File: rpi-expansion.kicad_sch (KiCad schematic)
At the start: 3 parts, among them J7 PinSocket_2x20_P2.54mm_Drill1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, J8 JST_SH_1x4_SM04B-SRSS-TB-LF-SN, J9 JST_SH_1x4_SM04B-SRSS-TB-LF-SN

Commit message: [#94684] Revise component placement
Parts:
- removed J7: PinSocket_2x20_P2.54mm_Drill1.02mm, antmicro-footprints:PinSocket_2x20_P2.54mm_Drill1.02mm, symbol antmicroGenericPinSockets:PinSocket_2x20_P2.54mm_Drill1.02mm
- added J7: PinHeader_2x20_P2.54mm_Drill1.1mm, antmicro-footprints:PinHeader_2x20_P2.54mm_Drill1.1mm, symbol antmicroGenericPinHeaders:PinHeader_2x20_P2.54mm_Drill1.1mm
- added R4, R5, R6, R7: R_0R_0402, antmicro-footprints:R_0402_1005Metric, symbol antmicroResistors0402:R_0R_0402
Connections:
- net I2C_QWIIC.SCL: now reaches J9.1
- net I2C_QWIIC.SCL: now also J8.1
- net I2C_QWIIC.SDA: now reaches J9.2
- net I2C_QWIIC.SDA: now also J8.2
- net QWIIC_VCC2: now reaches J9.3
- net QWIIC_VCC2: now also R6.1, R7.1
- net GND: now reaches J9.4
- net GND: now also J8.4, J8.MP, J9.MP, J7.14, J7.20, J7.25, J7.30, J7.34, J7.39, J7.6, J7.9
- net QWIIC_VCC1: now reaches J8.3
- net QWIIC_VCC1: now also R4.1, R5.1
- new net +3V3: J7.1, R5.2, R7.2
- new net +5V: J7.2, J7.4, R4.2, R6.2
- new net GPIO4: J7.7
- new net I2C_RPI.SCL: J7.5
- new net I2C_RPI.SDA: J7.3
- new net SPI_RPI.CS0: J7.24
- new net SPI_RPI.CS1: J7.26
- new net SPI_RPI.MISO: J7.21
- new net SPI_RPI.MOSI: J7.19
- new net SPI_RPI.SCK: J7.23
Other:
- moved on the sheet: J8, J9

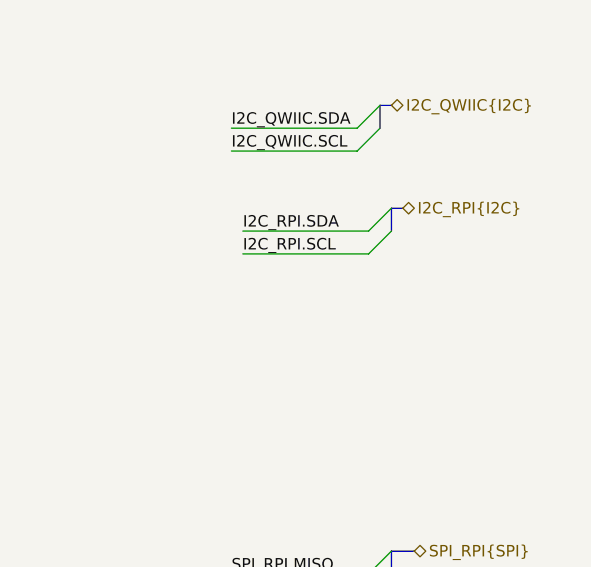
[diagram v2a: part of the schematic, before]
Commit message: [#94727] Add RMII, IOs, JTAG, UART, QSPI connection to MCU
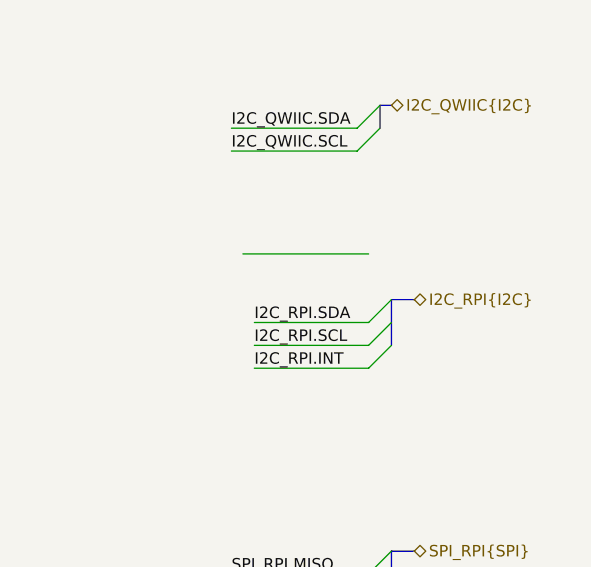
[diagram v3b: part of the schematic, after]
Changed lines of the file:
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@@
 	)
 	(bus_entry
-		(at 308.61 80.01)
+		(at 308.61 92.71)
 		(size -2.54 2.54)
 		(stroke
@@
 	)
 	(bus_entry
+		(at 308.61 95.25)
+		(size -2.54 2.54)
+		(stroke
+			(width 0)
+			(type default)
+		)
+	)
+	(bus_entry
 		(at 308.61 120.65)
 		(size -2.54 2.54)
@@
 	)
 	(bus_entry
-		(at 308.61 125.73)
+		(at 308.61 90.17)
 		(size -2.54 2.54)
 		(stroke
@@
 	)
 	(bus_entry
-		(at 308.61 123.19)
+		(at 308.61 125.73)
 		(size -2.54 2.54)
 		(stroke
@@
 	)
 	(bus_entry
-		(at 308.61 82.55)
+		(at 308.61 123.19)
 		(size -2.54 2.54)
 		(stroke
@@
 		)
 	)
+	(wire
+		(pts
+			(xy 306.07 92.71) (xy 293.37 92.71)
+		)
+		(stroke
+			(width 0)
+			(type default)
+		)
+	)
 	(bus
 		(pts
@@
 	(wire
 		(pts
+			(xy 306.07 95.25) (xy 293.37 95.25)
+		)
+		(stroke
+			(width 0)
+			(type default)
+		)
+	)
+	(wire
+		(pts
 			(xy 262.89 36.83) (xy 259.08 36.83)
 		)
@@
 		)
 	)
-	(bus
-		(pts
-			(xy 309.88 80.01) (xy 308.61 80.01)
-		)
-		(stroke
-			(width 0)
-			(type default)
-		)
-	)
 	(wire
 		(pts
@@
 	(wire
 		(pts
-			(xy 271.78 36.83) (xy 283.21 36.83)
+			(xy 306.07 97.79) (xy 293.37 97.79)
 		)
 		(stroke
@@
 	(wire
 		(pts
-			(xy 292.1 82.55) (xy 306.07 82.55)
+			(xy 271.78 36.83) (xy 283.21 36.83)
 		)
 		(stroke
@@
 	(bus
 		(pts
-			(xy 308.61 80.01) (xy 308.61 82.55)
+			(xy 307.34 68.58) (xy 307.34 71.12)
 		)
 		(stroke
@@
 		)
 	)
-	(bus
+	(wire
 		(pts
-			(xy 307.34 68.58) (xy 307.34 71.12)
+			(xy 259.08 36.83) (xy 259.08 31.75)
 		)
 		(stroke
@@
 	(wire
 		(pts
-			(xy 259.08 36.83) (xy 259.08 31.75)
+			(xy 123.19 104.14) (xy 134.62 104.14)
 		)
 		(stroke
@@
 		)
 	)
-	(wire
+	(bus
 		(pts
-			(xy 123.19 104.14) (xy 134.62 104.14)
+			(xy 311.15 90.17) (xy 308.61 90.17)
+		)
+		(stroke
+			(width 0)
+			(type default)
+		)
+	)
+	(bus
+		(pts
+			(xy 308.61 90.17) (xy 308.61 92.71)
 		)
 		(stroke
@@
 		)
 	)
+	(bus
+		(pts
+			(xy 308.61 92.71) (xy 308.61 95.25)
+		)
+		(stroke
+			(width 0)
+			(type default)
+		)
+	)
 	(wire
 		(pts
@@
 		)
 	)
-	(label "I2C_RPI.SCL"
-		(at 292.1 85.09 0)
-		(effects
-			(font
-				(size 1.27 1.27)
-			)
-			(justify left bottom)
-		)
-	)
 	(label "SPI_RPI.CS0"
 		(at 290.83 128.27 0)
@@
 		)
 	)
-	(label "I2C_RPI.SDA"
-		(at 292.1 82.55 0)
+	(label "I2C_RPI.INT"
+		(at 293.37 97.79 0)
 		(effects
 			(font
@@
 		)
 	)
+	(label "I2C_RPI.SDA"
+		(at 293.37 92.71 0)
+		(effects
+			(font
+				(size 1.27 1.27)
+			)
+			(justify left bottom)
+		)
+	)
 	(label "SPI_RPI.MISO"
 		(at 118.11 124.46 0)
@@
 		)
 	)
+	(label "I2C_RPI.SCL"
+		(at 293.37 95.25 0)
+		(effects
+			(font
+				(size 1.27 1.27)
+			)
+			(justify left bottom)
+		)
+	)
 	(label "I2C_RPI.SDA"
 		(at 123.19 101.6 0)
@@
 	(hierarchical_label "I2C_RPI{I2C}"
 		(shape bidirectional)
-		(at 309.88 80.01 0)
+		(at 311.15 90.17 0)
 		(effects
 			(font

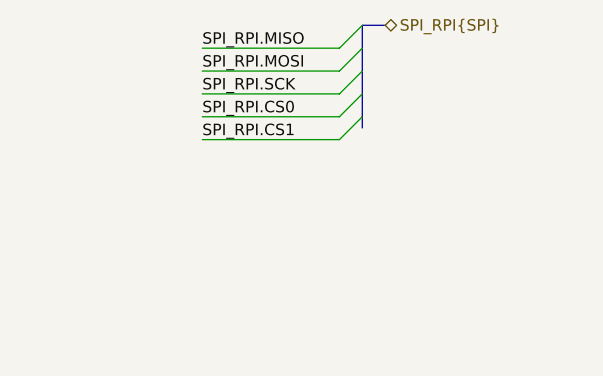
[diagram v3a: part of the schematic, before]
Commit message: [94727] Add remaining I2C buses
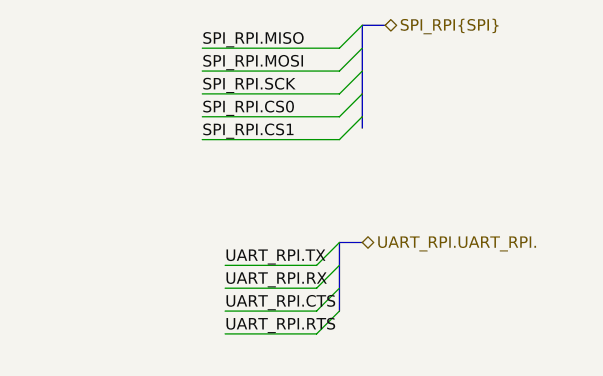
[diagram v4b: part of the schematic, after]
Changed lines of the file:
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@@
 	)
 	(bus_entry
+		(at 306.07 149.86)
+		(size -2.54 2.54)
+		(stroke
+			(width 0)
+			(type default)
+		)
+	)
+	(bus_entry
 		(at 308.61 120.65)
 		(size -2.54 2.54)
@@
 	)
 	(bus_entry
+		(at 306.07 142.24)
+		(size -2.54 2.54)
+		(stroke
+			(width 0)
+			(type default)
+		)
+	)
+	(bus_entry
+		(at 306.07 144.78)
+		(size -2.54 2.54)
+		(stroke
+			(width 0)
+			(type default)
+		)
+	)
+	(bus_entry
 		(at 308.61 123.19)
 		(size -2.54 2.54)
@@
 		)
 	)
+	(bus_entry
+		(at 306.07 147.32)
+		(size -2.54 2.54)
+		(stroke
+			(width 0)
+			(type default)
+		)
+	)
 	(wire
 		(pts
@@
 	(wire
 		(pts
+			(xy 293.37 147.32) (xy 303.53 147.32)
+		)
+		(stroke
+			(width 0)
+			(type default)
+		)
+	)
+	(wire
+		(pts
 			(xy 298.45 36.83) (xy 294.64 36.83)
 		)
@@
 		)
 	)
+	(bus
+		(pts
+			(xy 306.07 147.32) (xy 306.07 149.86)
+		)
+		(stroke
+			(width 0)
+			(type default)
+		)
+	)
 	(wire
 		(pts
@@
 	(wire
 		(pts
+			(xy 293.37 149.86) (xy 303.53 149.86)
+		)
+		(stroke
+			(width 0)
+			(type default)
+		)
+	)
+	(wire
+		(pts
 			(xy 144.78 101.6) (xy 148.59 101.6)
 		)
@@
 	(wire
 		(pts
+			(xy 293.37 144.78) (xy 303.53 144.78)
+		)
+		(stroke
+			(width 0)
+			(type default)
+		)
+	)
+	(wire
+		(pts
 			(xy 290.83 128.27) (xy 306.07 128.27)
 		)
@@
 	(wire
 		(pts
+			(xy 293.37 152.4) (xy 303.53 152.4)
+		)
+		(stroke
+			(width 0)
+			(type default)
+		)
+	)
+	(wire
+		(pts
 			(xy 267.97 39.37) (xy 271.78 39.37)
 		)
@@
 		)
 	)
+	(bus
+		(pts
+			(xy 308.61 142.24) (xy 306.07 142.24)
+		)
+		(stroke
+			(width 0)
+			(type default)
+		)
+	)
 	(wire
 		(pts
@@
 		)
 	)
+	(bus
+		(pts
+			(xy 306.07 142.24) (xy 306.07 144.78)
+		)
+		(stroke
+			(width 0)
+			(type default)
+		)
+	)
 	(wire
 		(pts
@@
 		)
 	)
+	(bus
+		(pts
+			(xy 306.07 144.78) (xy 306.07 147.32)
+		)
+		(stroke
+			(width 0)
+			(type default)
+		)
+	)
 	(image
 		(at 64.77 123.19)
@@
 		)
 	)
+	(label "UART_RPI.RTS"
+		(at 293.37 152.4 0)
+		(effects
+			(font
+				(size 1.27 1.27)
+			)
+			(justify left bottom)
+		)
+	)
 	(label "I2C_RPI.SDA"
 		(at 293.37 92.71 0)
@@
 		)
 	)
+	(label "UART_RPI.RX"
+		(at 293.37 147.32 0)
+		(effects
+			(font
+				(size 1.27 1.27)
+			)
+			(justify left bottom)
+		)
+	)
+	(label "UART_RPI.TX"
+		(at 293.37 144.78 0)
+		(effects
+			(font
+				(size 1.27 1.27)
+			)
+			(justify left bottom)
+		)
+	)
 	(label "SPI_RPI.MISO"
 		(at 118.11 124.46 0)
@@
 		)
 	)
+	(label "UART_RPI.CTS"
+		(at 293.37 149.86 0)
+		(effects
+			(font
+				(size 1.27 1.27)
+			)
+			(justify left bottom)
+		)
+	)
 	(label "I2C_RPI.SDA"
 		(at 123.19 101.6 0)
@@
 		(effects
 			(font
+				(size 1.27 1.27)
+			)
+			(justify left)
+		)
+	)
+	(hierarchical_label "UART_RPI.UART_RPI."
+		(shape bidirectional)
+		(at 308.61 142.24 0)
+		(effects
+			(font

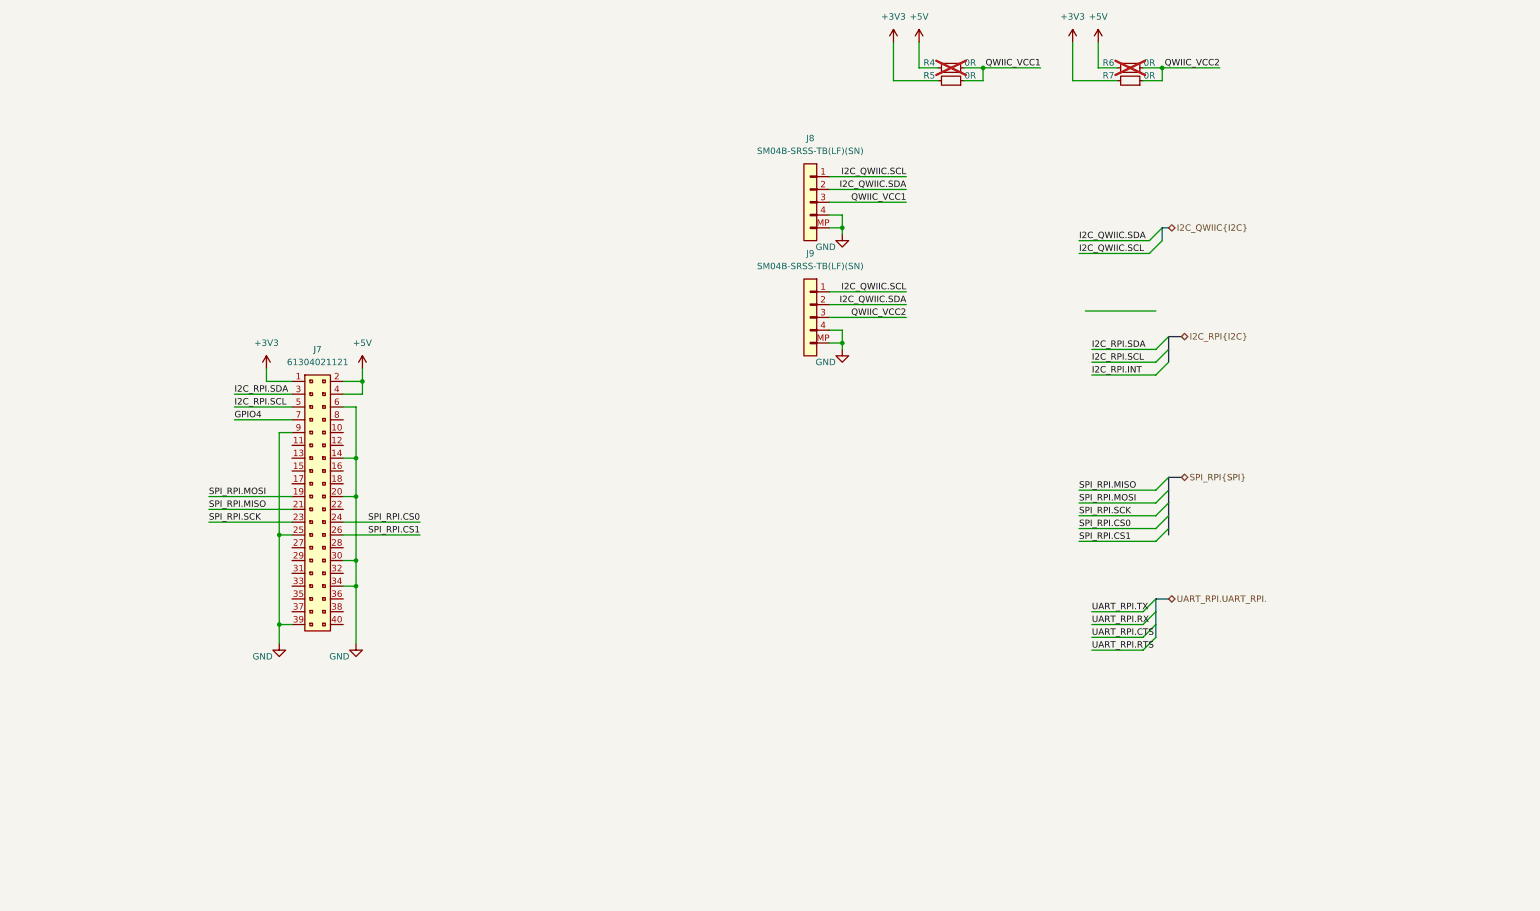
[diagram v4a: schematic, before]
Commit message: [#95036] Reconnect power flags, add GPIOs to RPI connector
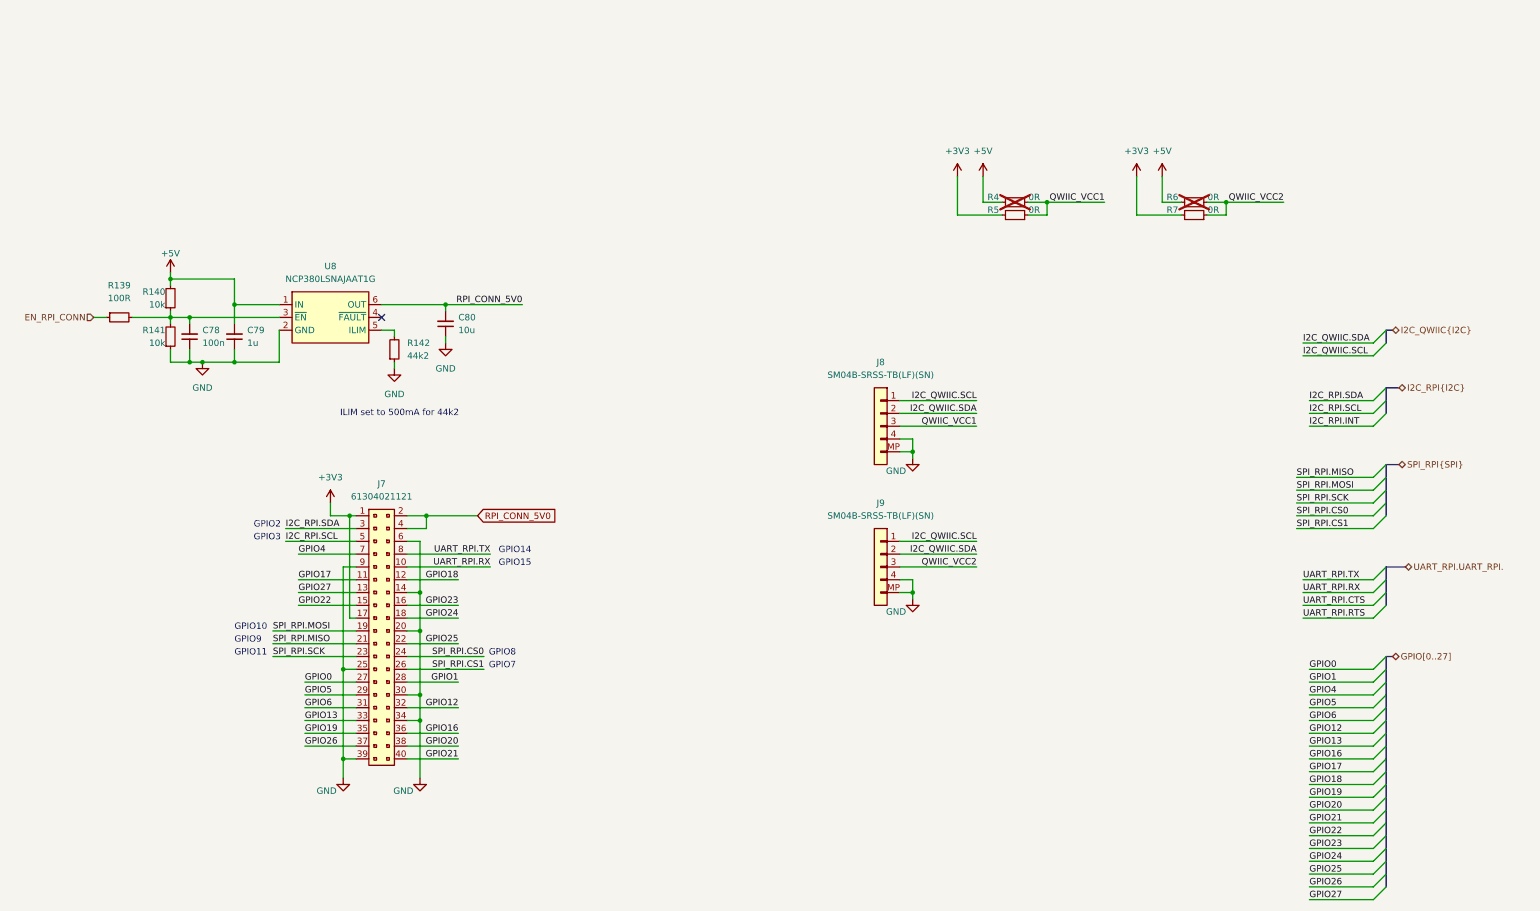
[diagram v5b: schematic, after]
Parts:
- added C78: C_100n_0402, antmicro-footprints:C_0402_1005Metric, symbol antmicroCapacitors0402:C_100n_0402
- added C79: C_1u_0402, antmicro-footprints:C_0402_1005Metric, symbol antmicroCapacitors0402:C_1u_0402
- added C80: C_10u_0402, antmicro-footprints:C_0402_1005Metric, symbol antmicroCapacitors0402:C_10u_0402
- added R139: R_100R_0402, antmicro-footprints:R_0402_1005Metric, symbol antmicroResistors0402:R_100R_0402
- added R140, R141: R_10k_0402, antmicro-footprints:R_0402_1005Metric, symbol antmicroResistors0402:R_10k_0402
- added R142: R_44k2_0402, antmicro-footprints:R_0402_1005Metric, symbol antmicroResistors0402:R_44k2_0402
- added U8: NCP380LSNAJAAT1G, antmicro-footprints:SOT-23-6, symbol antmicroPMICPowerDistributionSwitchesLoadDrivers:NCP380LSNAJAAT1G
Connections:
- net +3V3: now also J7.17
- net +5V: now also C79.2, R140.2, U8.1 (IN); no longer J7.2, J7.4
- net GND: now also C78.1, C79.1, C80.1, R141.1, R142.1, U8.2 (GND)
- net UART_RPI.RX: now also J7.10
- net UART_RPI.TX: now also J7.8
- net GPIO17: now reaches J7.11
- net GPIO18: now reaches J7.12
- net GPIO27: now reaches J7.13
- net GPIO22: now reaches J7.15
- net GPIO23: now reaches J7.16
- net GPIO24: now reaches J7.18
- net GPIO25: now reaches J7.22
- net GPIO0: now reaches J7.27
- net GPIO1: now reaches J7.28
- net GPIO5: now reaches J7.29
- net GPIO6: now reaches J7.31
- net GPIO12: now reaches J7.32
- net GPIO13: now reaches J7.33
- net GPIO19: now reaches J7.35
- net GPIO16: now reaches J7.36
- net GPIO26: now reaches J7.37
- net GPIO20: now reaches J7.38
- net GPIO21: now reaches J7.40
- new net: C78.2, R139.2, R140.1, R141.2, U8.3 (~{EN})
- new net: R142.2, U8.5 (ILIM)
- new net EN_RPI_CONN: R139.1
- new net RPI_CONN_5V0: C80.2, J7.2, J7.4, U8.6 (OUT)
- no-connect marks 0 -> 1
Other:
- note added: "GPIO10"
- note added: "GPIO11"
- note added: "GPIO14"
- note added: "GPIO15"
- note added: "GPIO2"
- note added: "GPIO3"
- note added: "GPIO7"
- note added: "GPIO8"
- note added: "GPIO9"
- note added: "ILIM set to 500mA for 44k2"
- moved on the sheet: J7, J8, J9, R4, R5, R6, R7

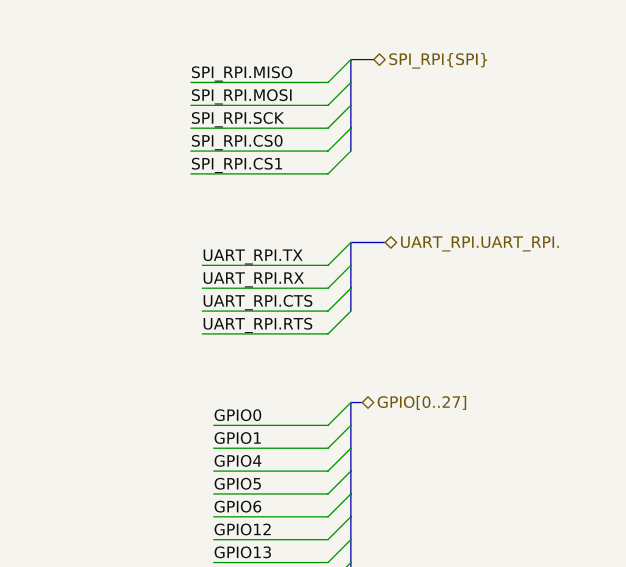
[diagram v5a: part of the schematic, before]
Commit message: [#95036] Manage I2C, UART, SPI interfaces for RPI and PMOD connectors
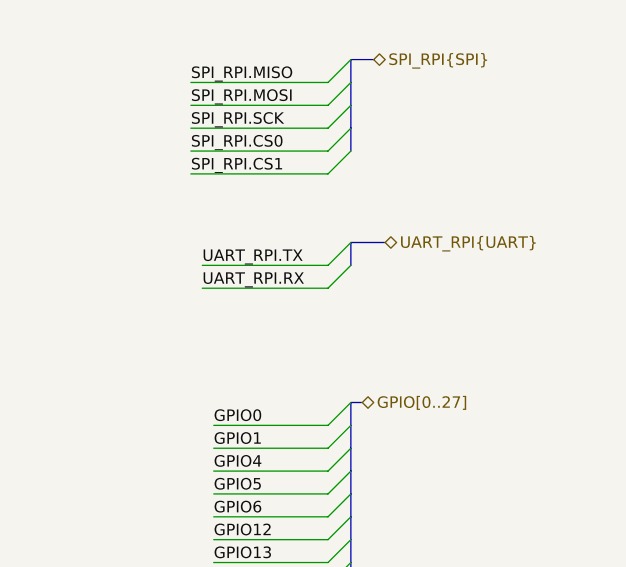
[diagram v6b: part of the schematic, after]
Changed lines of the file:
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@@
 	)
 	(bus_entry
-		(at 351.79 143.51)
-		(size -2.54 2.54)
-		(stroke
-			(width 0)
-			(type default)
-		)
-	)
-	(bus_entry
 		(at 351.79 158.75)
 		(size -2.54 2.54)
@@
 		)
 	)
-	(bus_entry
-		(at 351.79 140.97)
-		(size -2.54 2.54)
-		(stroke
-			(width 0)
-			(type default)
-		)
-	)
 	(wire
 		(pts
@@
 		)
 	)
-	(bus
-		(pts
-			(xy 351.79 140.97) (xy 351.79 143.51)
-		)
-		(stroke
-			(width 0)
-			(type default)
-		)
-	)
 	(wire
 		(pts
@@
 	(wire
 		(pts
-			(xy 335.28 143.51) (xy 349.25 143.51)
-		)
-		(stroke
-			(width 0)
-			(type default)
-		)
-	)
-	(wire
-		(pts
 			(xy 157.48 128.27) (xy 161.29 128.27)
 		)
@@
 	(wire
 		(pts
-			(xy 335.28 146.05) (xy 349.25 146.05)
-		)
-		(stroke
-			(width 0)
-			(type default)
-		)
-	)
-	(wire
-		(pts
 			(xy 132.08 88.9) (xy 132.08 95.25)
 		)
@@
 		)
 	)
-	(bus
-		(pts
-			(xy 351.79 138.43) (xy 351.79 140.97)
-		)
-		(stroke
-			(width 0)
-			(type default)
-		)
-	)
 	(wire
 		(pts
@@
 		)
 	)
-	(label "UART_RPI.RTS"
-		(at 335.28 146.05 0)
-		(effects
-			(font
-				(size 1.27 1.27)
-			)
-			(justify left bottom)
-		)
-	)
 	(label "I2C_RPI.SDA"
 		(at 336.55 102.87 0)
@@
 		)
 	)
-	(label "UART_RPI.CTS"
-		(at 335.28 143.51 0)
-		(effects
-			(font
-				(size 1.27 1.27)
-			)
-			(justify left bottom)
-		)
-	)
 	(label "I2C_RPI.SDA"
 		(at 133.35 128.27 0)
@@
 		)
 	)
-	(hierarchical_label "UART_RPI.UART_RPI."
+	(hierarchical_label "UART_RPI{UART}"
 		(shape bidirectional)
 		(at 355.6 135.89 0)
